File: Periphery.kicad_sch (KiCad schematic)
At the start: 11 parts, among them SW1 Mitsumi R-667996, SW2 Mitsumi R-667996, U2 IS31FL3726A-QFLS4, U3 THVD1420DRLR, U4 RS31340B

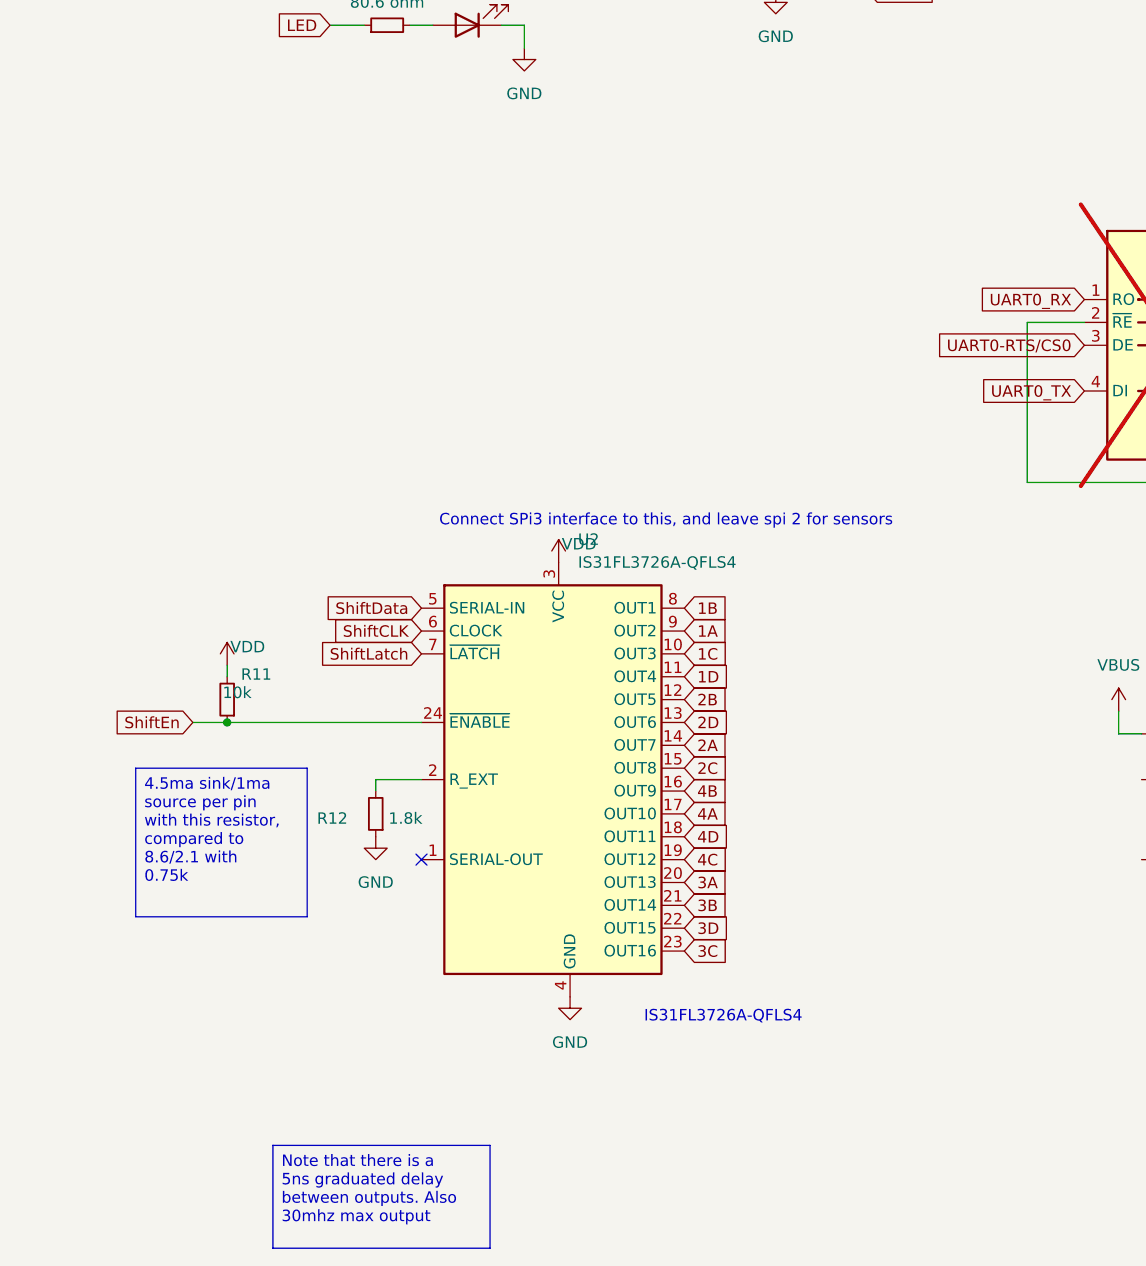
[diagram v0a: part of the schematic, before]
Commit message: Replaced LED driver with 2 shift registers
My initial approach from the first version was better design, I need 80+ mhz to get adequate PWM signals.
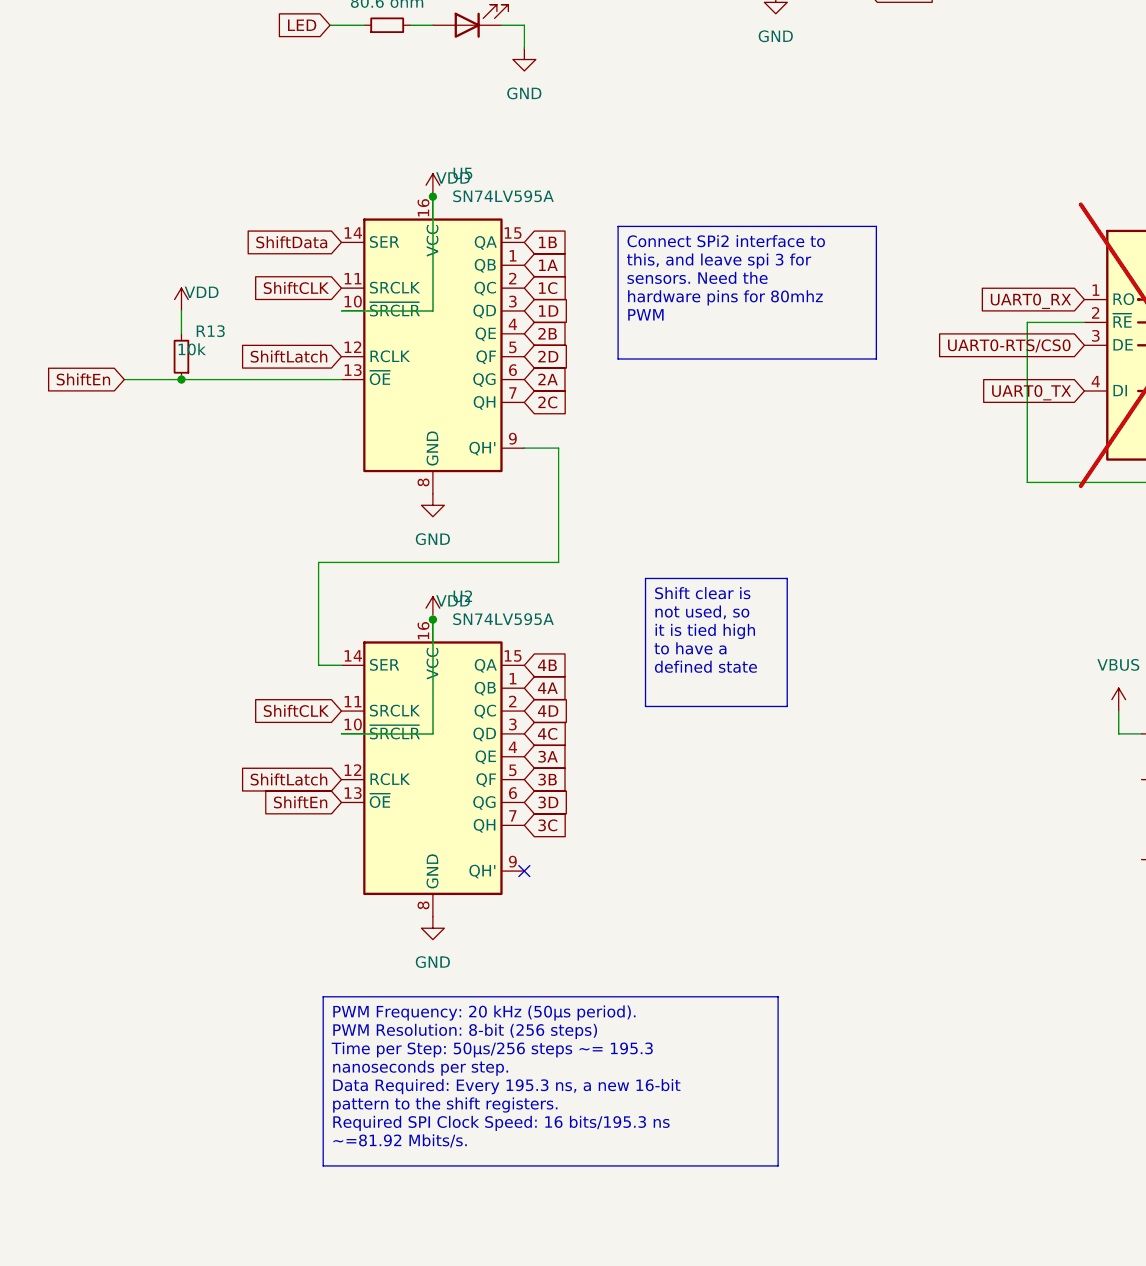
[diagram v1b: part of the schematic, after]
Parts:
- removed R11: 10k, Resistor_SMD:R_0402_1005Metric, symbol Device:R_Small
- removed R12: 1.8k, Resistor_SMD:R_0402_1005Metric, symbol Device:R_Small
- removed U2: IS31FL3726A-QFLS4, Package_DFN_QFN:QFN-24-1EP_4x4mm_P0.5mm_EP2.7x2.7mm, symbol custom_Driver_LED:IS31FL3726A
- added R13: 10k, Resistor_SMD:R_0402_1005Metric, symbol Device:R_Small
- added U2, U5: SN74LV595A, symbol 74xx:74HC595
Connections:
- net 1A: now also U5.1 (QB)
- net 1B: now also U5.15 (QA)
- net 1C: now also U5.2 (QC)
- net 1D: now also U5.3 (QD)
- net 2A: now also U5.6 (QG)
- net 2B: now also U5.4 (QE)
- net 2C: now also U5.7 (QH)
- net 2D: now also U5.5 (QF)
- net 3A: now also U2.4 (QE)
- net 3B: now also U2.5 (QF)
- net 3C: now also U2.7 (QH)
- net 3D: now also U2.6 (QG)
- net 4A: now also U2.1 (QB)
- net 4B: now also U2.15 (QA)
- net 4C: now also U2.3 (QD)
- net 4D: now also U2.2 (QC)
- net GND: now also U2.8 (GND), U5.8 (GND); no longer U4.GND
- net ShiftCLK: now also U2.11 (SRCLK), U5.11 (SRCLK)
- net ShiftData: now also U5.14 (SER)
- net ShiftEn: now also R13.1, U2.13 (~{OE}), U5.13 (~{OE})
- net ShiftLatch: now also U2.12 (RCLK), U5.12 (RCLK)
- net VDD: now also R13.2, U2.10 (~{SRCLR}), U2.16 (VCC), U5.10 (~{SRCLR}), U5.16 (VCC)
- new net: U2.14 (SER), U5.9 (QH')
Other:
- note removed: "Connect SPi3 interface to this, and leave spi 2 for sensors"
- note removed: "IS31FL3726A-QFLS4"

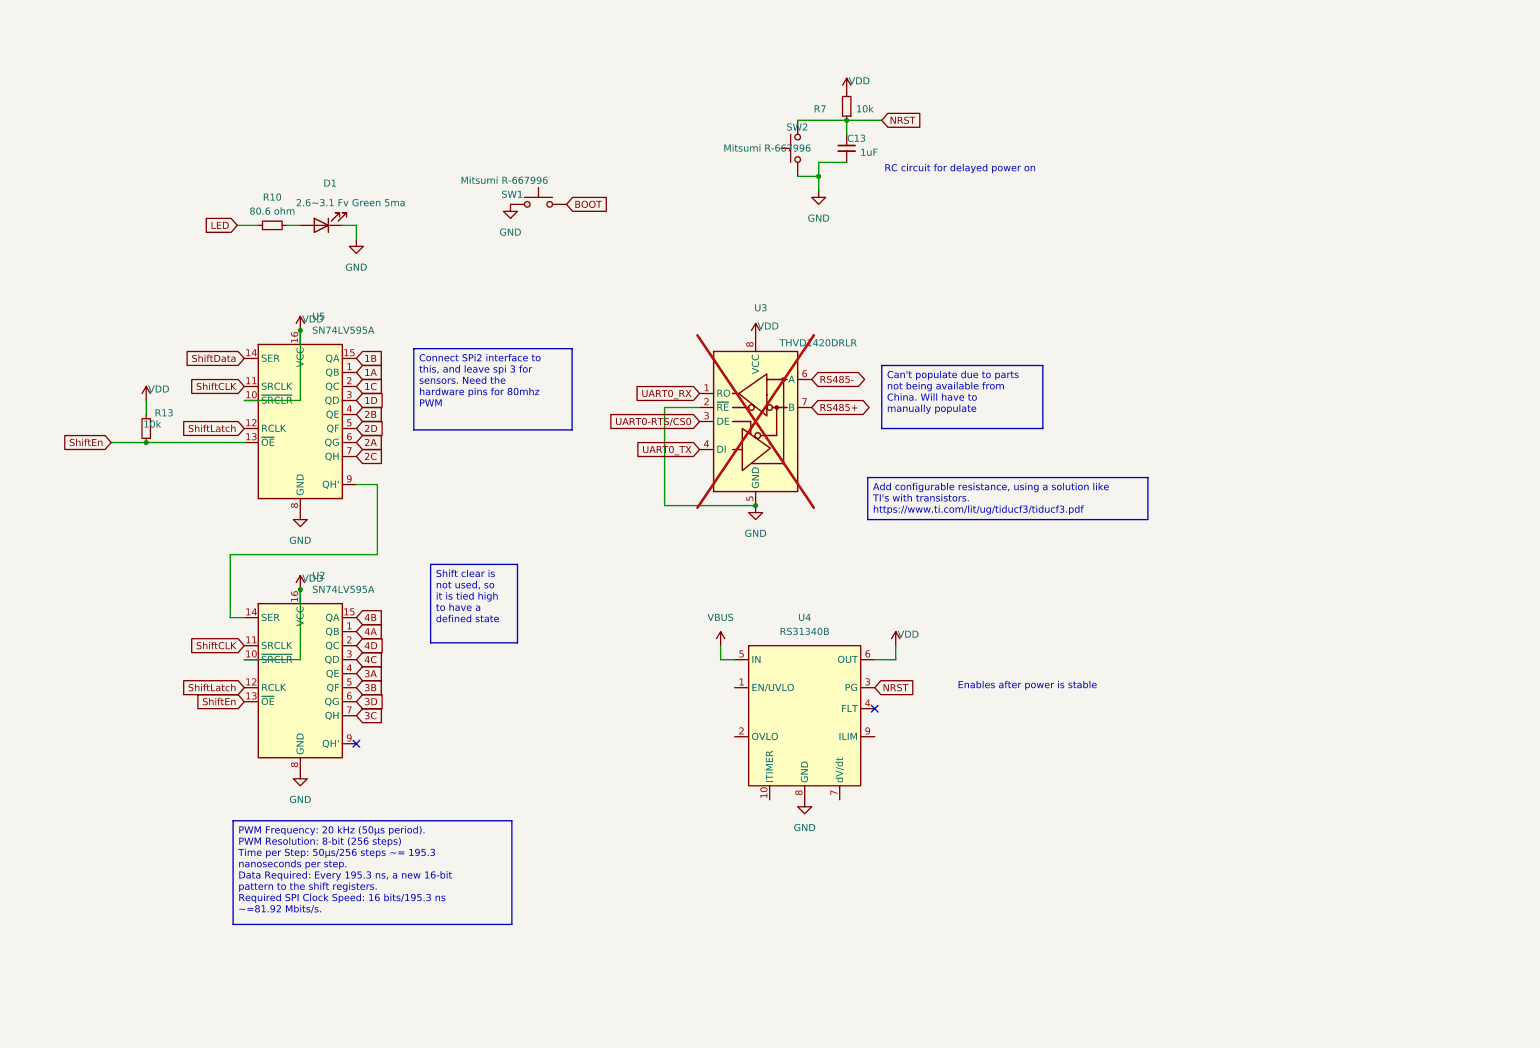
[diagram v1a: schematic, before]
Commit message: Added configurable termination with analog switch
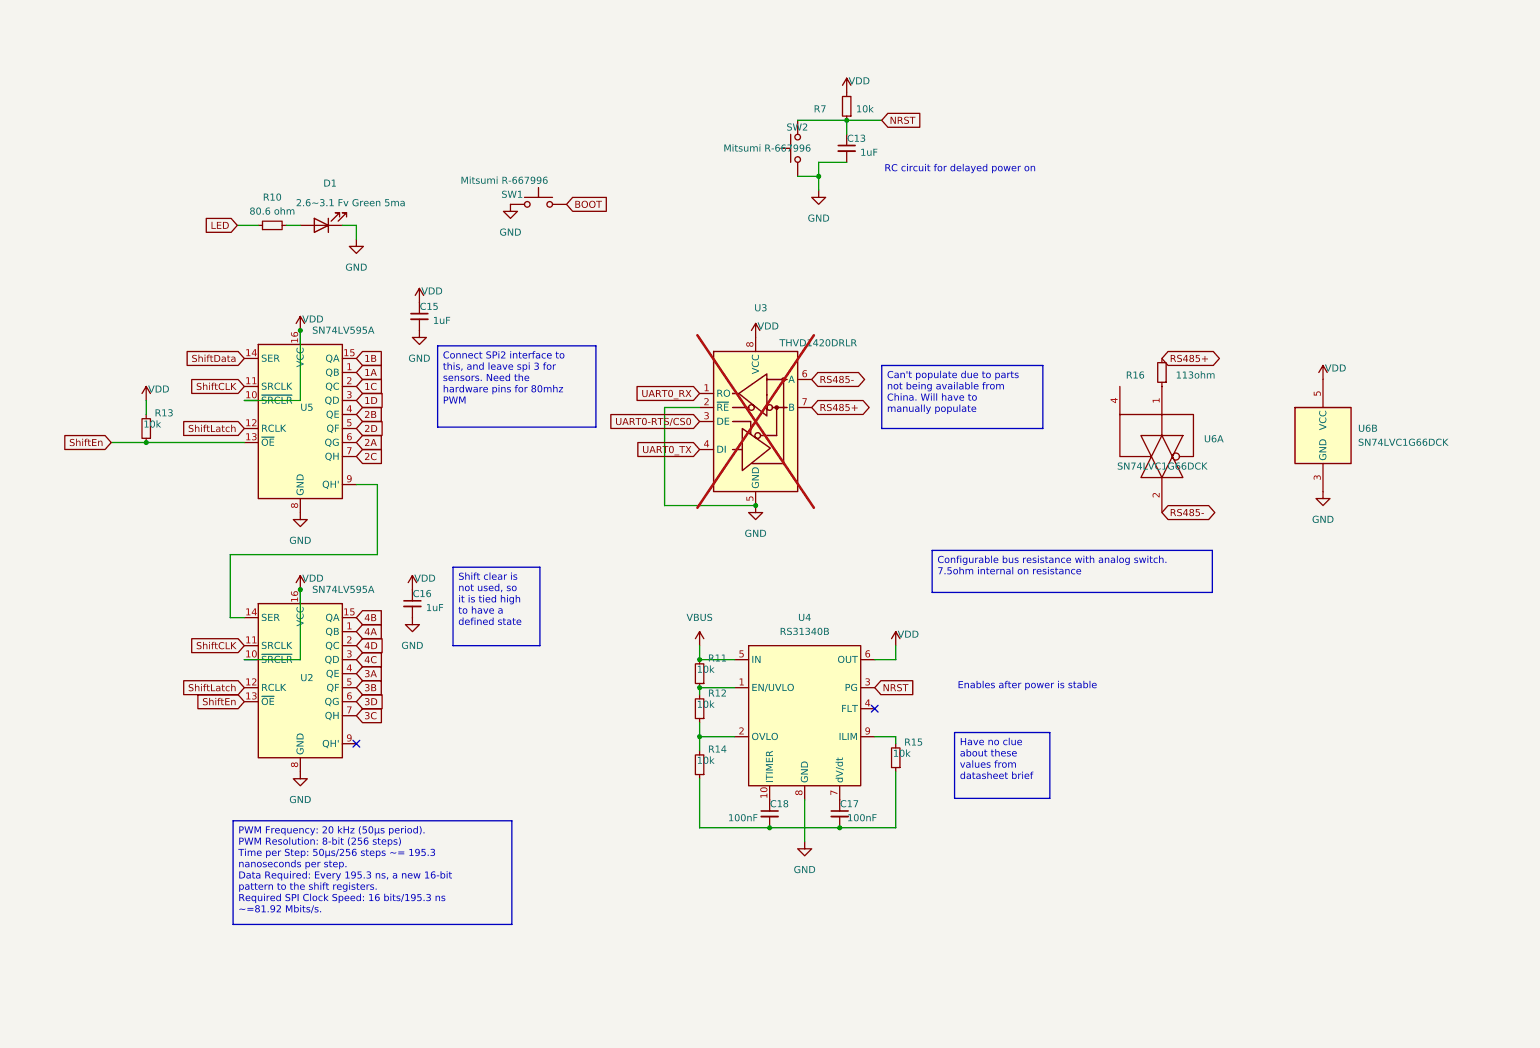
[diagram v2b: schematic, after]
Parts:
- added C15, C16: 1uF, Capacitor_SMD:C_0402_1005Metric, symbol Device:C_Small
- added C17, C18: 100nF, Capacitor_SMD:C_0402_1005Metric, symbol Device:C_Small
- added R11, R12, R14, R15: 10k, Resistor_SMD:R_0402_1005Metric, symbol Device:R_Small
- added R16: 113ohm, Resistor_SMD:R_0402_1005Metric, symbol Device:R_Small
- added U6: SN74LVC1G66DCK, Package_TO_SOT_SMD:SOT-353_SC-70-5, symbol 74xGxx:74LVC1G66
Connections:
- net GND: now also C15.2, C16.2, U6.3 (GND)
- net RS485+: now also R16.2
- net RS485-: now also U6.2
- net VBUS: now also R11.2
- net VDD: now also C15.1, C16.1, U6.5 (VCC)
- net at U4.1 (EN/UVLO): now also R11.1, R12.2
- net at U4.10 (ITIMER): now also C18.1
- net at U4.2 (OVLO): now also R12.1, R14.2
- net at U4.7 (dV/dt): now also C17.1
- net at U4.9 (ILIM): now also R15.2
- new net: R16.1, U6.1
- new net: C17.2, C18.2, R14.1, R15.1

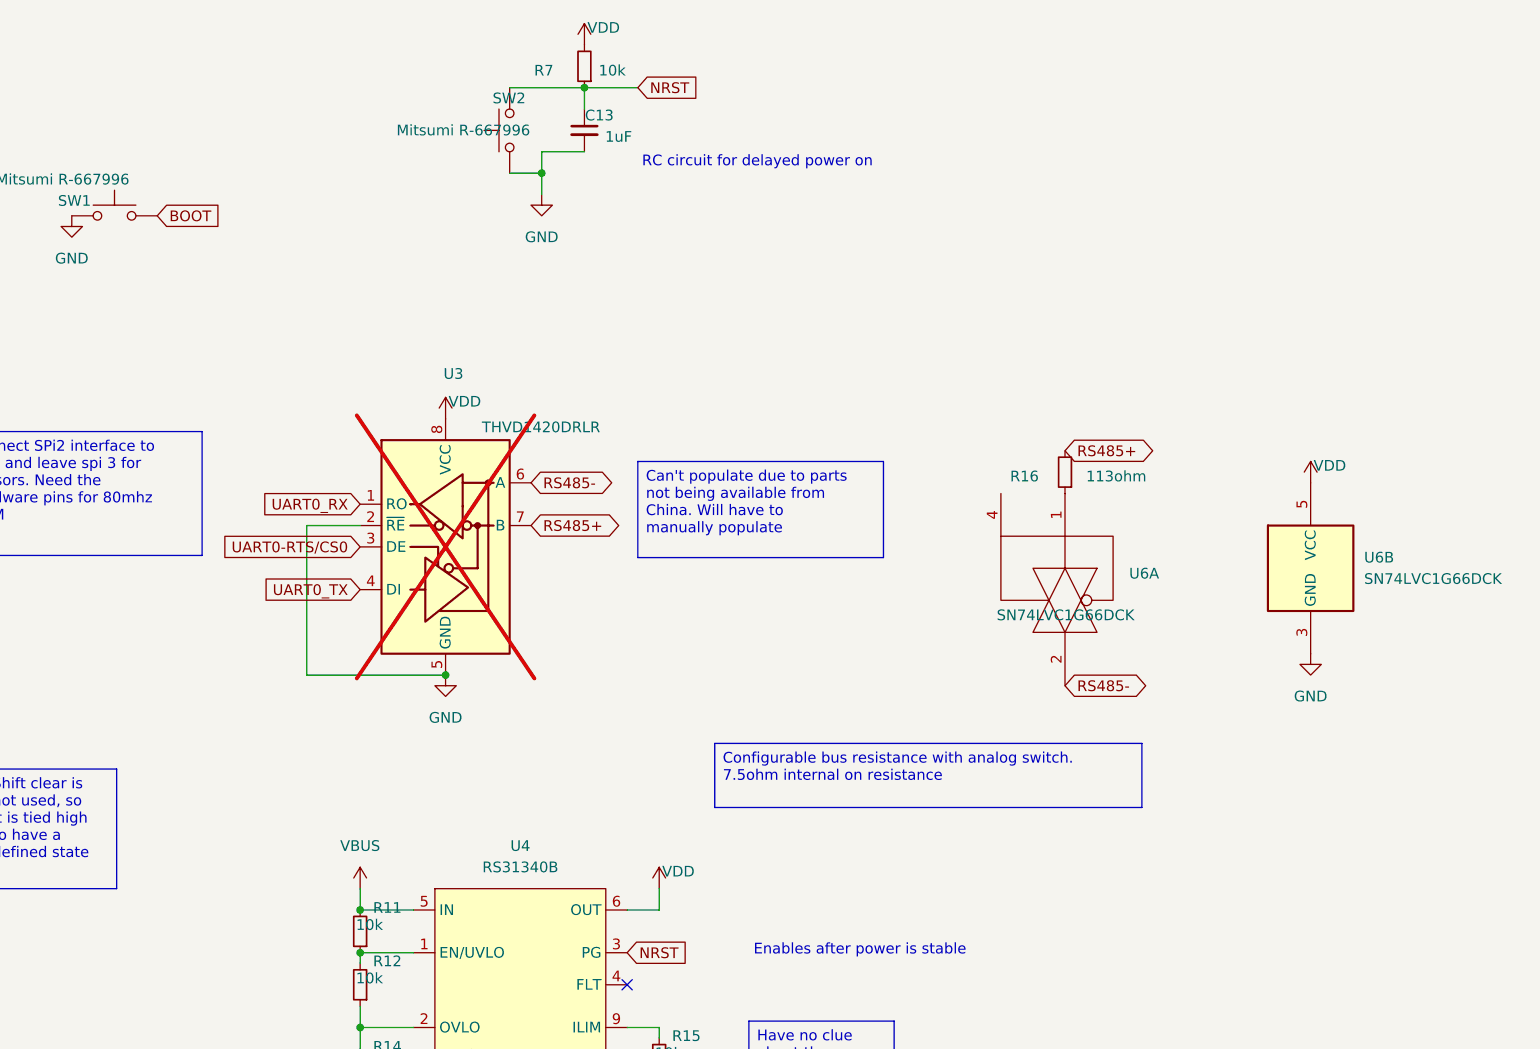
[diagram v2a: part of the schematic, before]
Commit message: Added shift reg footprints
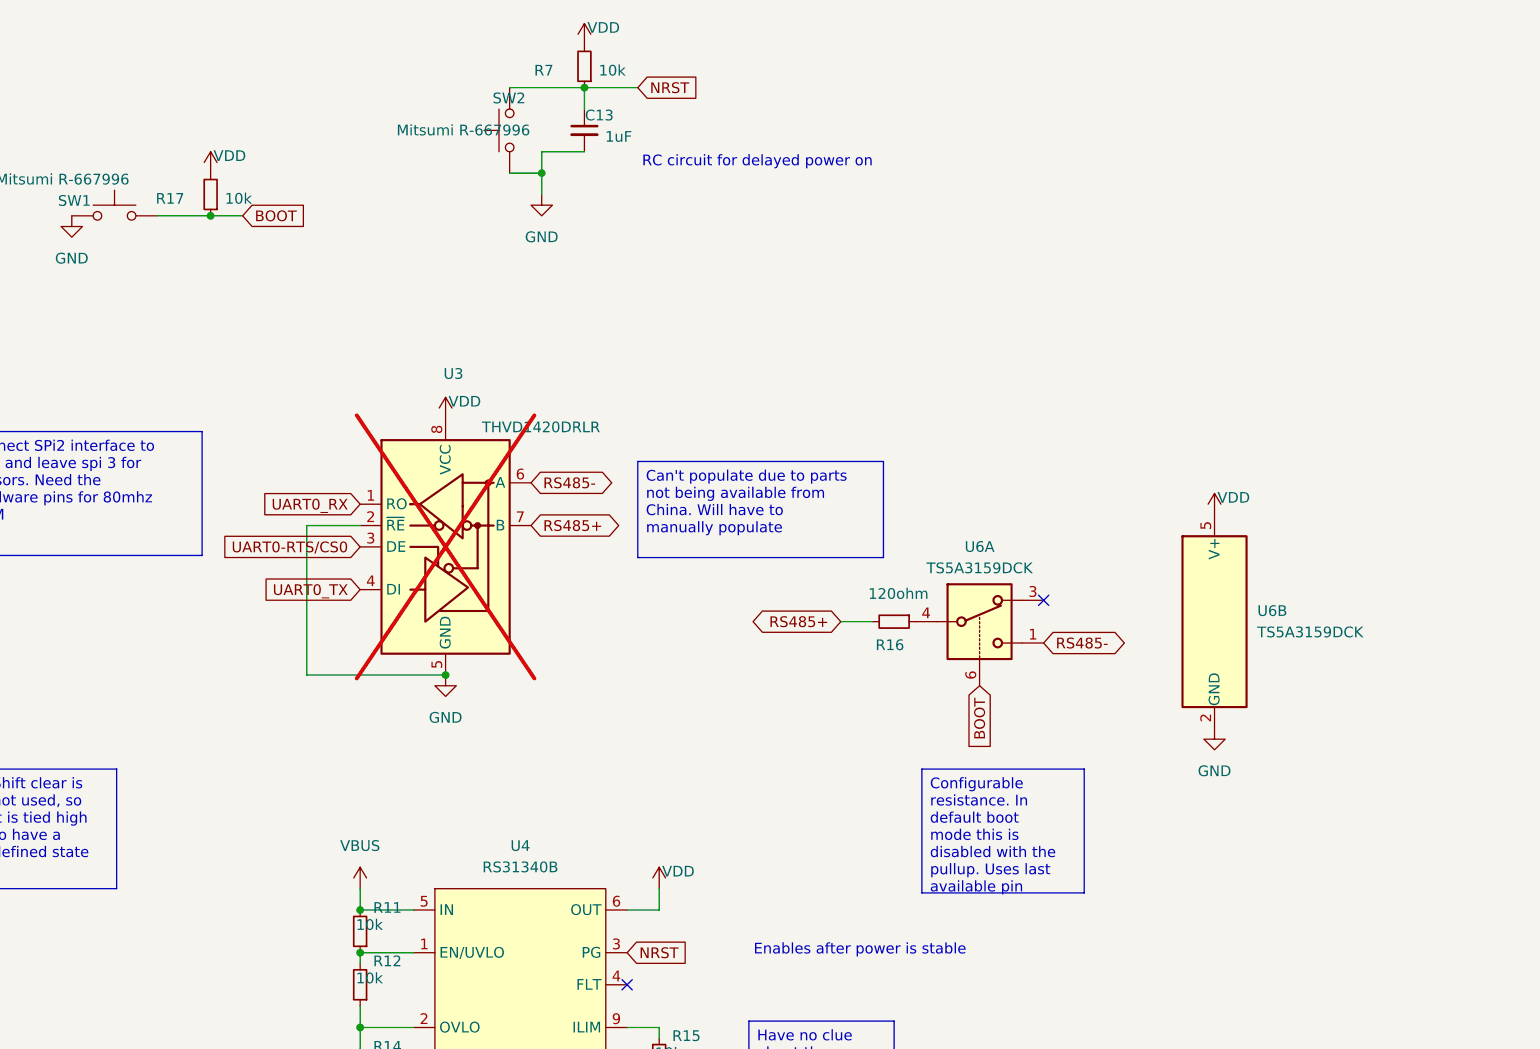
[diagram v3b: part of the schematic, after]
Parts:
- removed U6: SN74LVC1G66DCK, Package_TO_SOT_SMD:SOT-353_SC-70-5, symbol 74xGxx:74LVC1G66
- added R17: 10k, Resistor_SMD:R_0402_1005Metric, symbol Device:R_Small
- added U6: TS5A3159DCK, Package_TO_SOT_SMD:SOT-363_SC-70-6, symbol Analog_Switch:TS5A3159DCK
- R16: value 113ohm -> 120ohm
- U2, U5: footprint (none) -> Package_DFN_QFN:DHVQFN-16-1EP_2.5x3.5mm_P0.5mm_EP1x2mm
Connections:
- net BOOT: now also R17.1, U6.6
- net GND: now also U6.2 (GND)
- net RS485-: now also U6.1
- net VDD: now also R17.2, U6.5 (V+)
- net at R16.1: now also U6.4
- no-connect marks 2 -> 3
